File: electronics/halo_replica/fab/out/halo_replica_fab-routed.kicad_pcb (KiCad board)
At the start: 4 copper layers, 30 x 30 mm, 45 parts, among them J1 VOICE COIL / SOUNDER, J2 NFC COIL 13.56MHz, J3 SWD (nRST SWDIO SWCLK GND VBA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, U1 nRF52832-QFAA-R, U2 MIC94090YC6 (0.5 uA, 1.5 A), U3 MX25R3235F 32Mb 1.65-3.6V, U4 SC7A20 3-axis, LGA-12, U5 MAX98357A class-D, TQFN-16, X1 32MHz 10ppm CL=8pF, X2 32.768kHz 20ppm CL=12.5pF

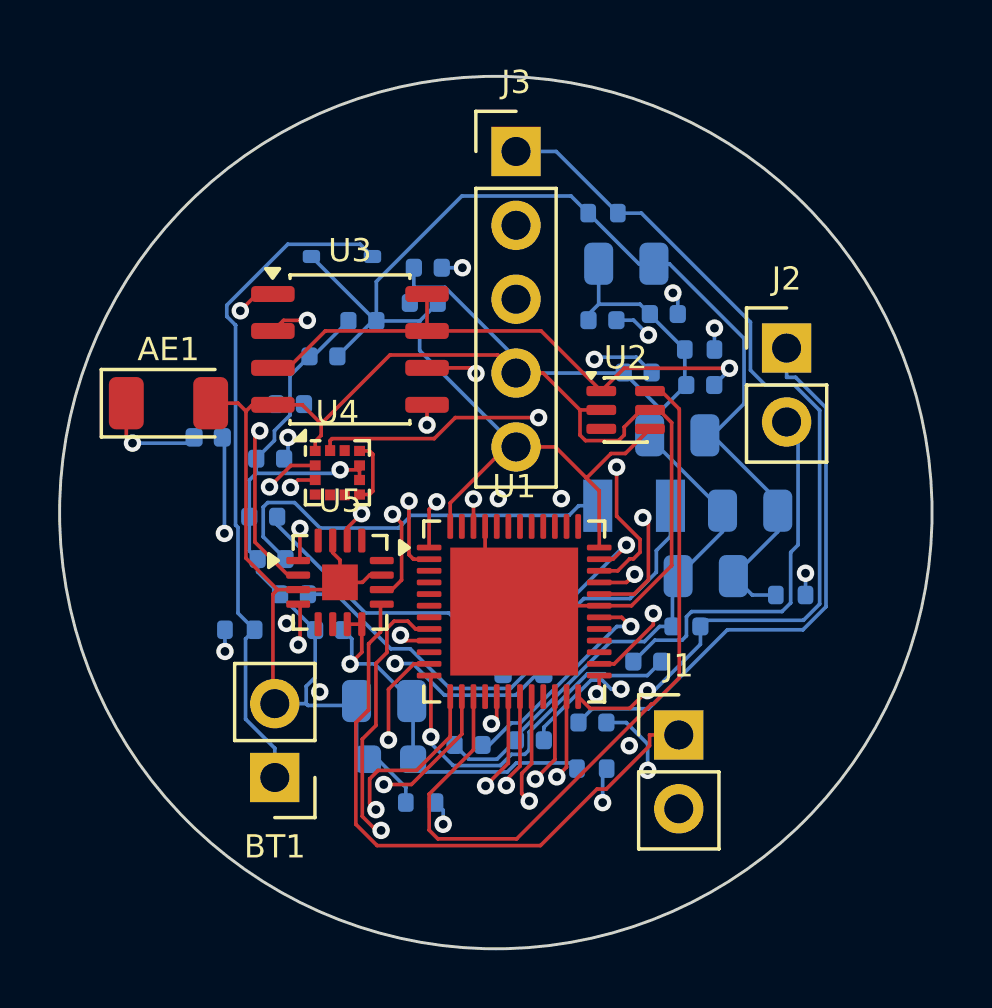
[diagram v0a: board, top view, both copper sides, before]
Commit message: checkpoint: land every AirTag lane's in-flight work before pausing them
Leif: "we should focus on the microduck and not the airtag so the airtag stuff
can wait stop the airtag stuff so we easily can resume it later."

This commit exists so that stopping those sessions loses NOTHING. 25 files were
uncommitted across the halo replica when the pause was called, including a
modified electronics/halo_replica/tools/c_register.py and the KiCad fab and
schematic outputs. They are committed as found, NOT because they are finished.
Whoever resumes should read this diff first.

WHY THE PAUSE, measured rather than asserted:
  load average 13.48 on 8 cores
  swap 5648 MB used of 6144 MB - 495 MB free of 8 GB physical
  AirTag lanes: 14 claude processes, 71.6 % CPU combined
  microduck:     2 processes, ~0 % CPU
darkpkg/SCALE.md records two kernel panics this week at this swap pressure. The
AirTag work was essentially the whole load, and a panic would have taken down the
microduck lanes that are mid-print on two printers.

RESUME-AIRTAG.md lists every lane that was live with its role and age, and
RESUME-AIRTAG-briefs.txt holds each process's verbatim launch prompt so a lane can
be brought back exactly as it was.

Not resumed because it is finished: L10 BLIND RIM COUNT, complete and pushed on
branch rimblind-99cab5fe (metrology/rimcount/R00-R04).

Co-Authored-By: Claude Opus 5 (1M context) <noreply@anthropic.com>
Claude-Session: https://claude.ai/code/session_013nSJSd43jHJX8fmes4smsQ
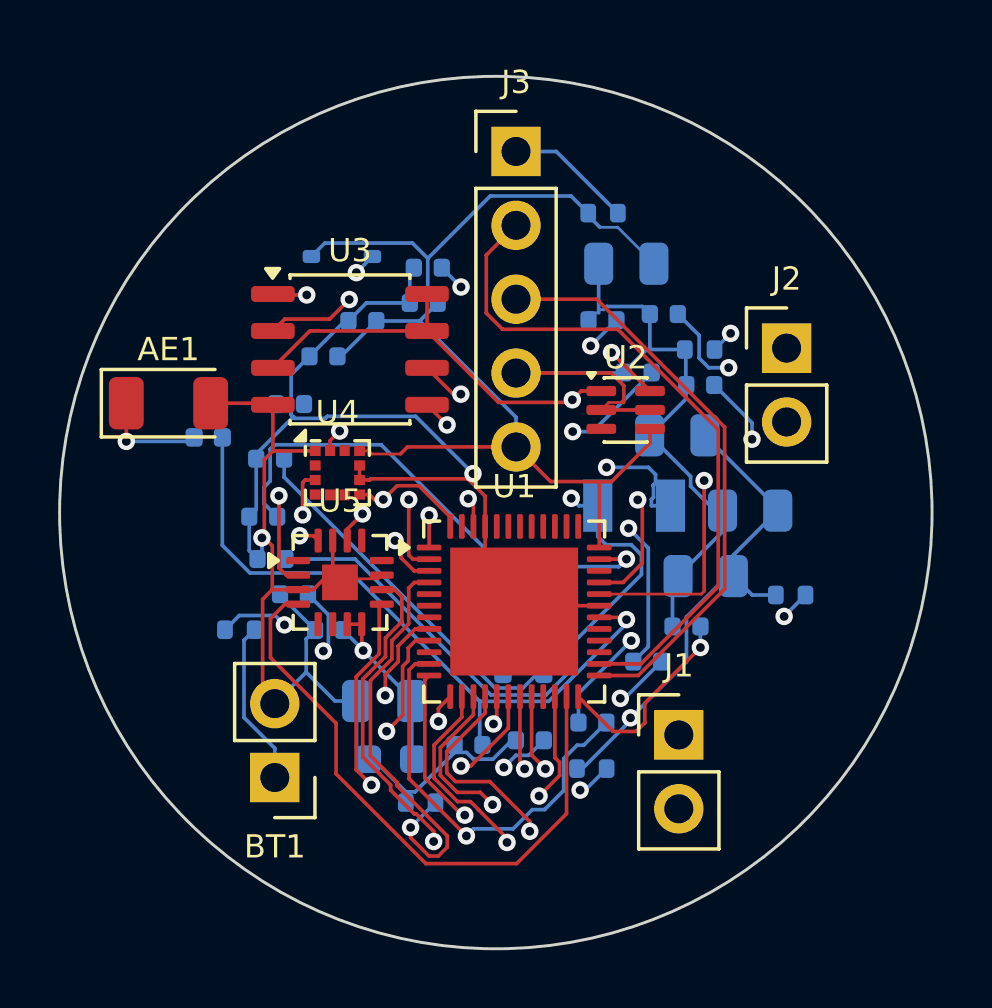
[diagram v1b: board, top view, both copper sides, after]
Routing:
- net XC1: track 37.5 -> 12.9 mm, vias 3 -> 0
- net I2S_BCLK: track 0.00 -> 23.5 mm, vias 0 -> 2
- net XL1: track 17.5 -> 35.2 mm, vias 1 -> 2
- net ACC_SDA: track 38.3 -> 20.8 mm, vias 4 -> 2
- net ACC_SCL: track 40.5 -> 23.5 mm
- net I2S_DIN: track 18.8 -> 3.78 mm, vias 3 -> 1
- net VBAT_SENSE: track 11.7 -> 25.7 mm
- net VBAT: track 109.3 -> 95.8 mm, vias 3 -> 5
- net GND: track 117.8 -> 104.7 mm, vias 1 -> 2
- net FLASH_nCS: track 24.4 -> 36.4 mm
- net AMP_nSD: track 15.3 -> 21.4 mm, vias 2 -> 0
- net SPI_MOSI: track 17.6 -> 23.3 mm
- net SWDIO: track 18.3 -> 23.7 mm, vias 1 -> 0
- net SWDCLK: track 15.4 -> 20.1 mm, vias 1 -> 0
- net VFLASH: track 19.5 -> 23.4 mm, vias 1 -> 2
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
